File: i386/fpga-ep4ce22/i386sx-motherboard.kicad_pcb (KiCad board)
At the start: 6 copper layers, 88.8 x 70.2 mm, 148 parts, among them J1 HR911105A, J2 PJ-063AH 12V, J3 JTAG, J4 SPI ISP, J5 UART, U1 NG80386SX-20, U10 TLV62569DBVR VCCAUX, U11 SN74LVC8T245PWR, U12 SN74LVC8T245PWR, U13 SN74LVC8T245PWR, U14 SN74LVC8T245PWR, U15 SN74LVC8T245PWR, U16 SN74LVC8T245PWR, U2 SN74AHCT1G125DBVR, U3 EP4CE22F17C8N, U4 W9825G6KH-6I, U5 W25Q64FVDAIG (DIP-8, socketed), U6 LAN8720A-CP-TR, U7 TPS5430DDAR 12->5V, U8 TPS54620RGYR 12->3V3, U9 TPS62130RGTR VCCINT, Y1 25MHz XO, Y2 25MHz

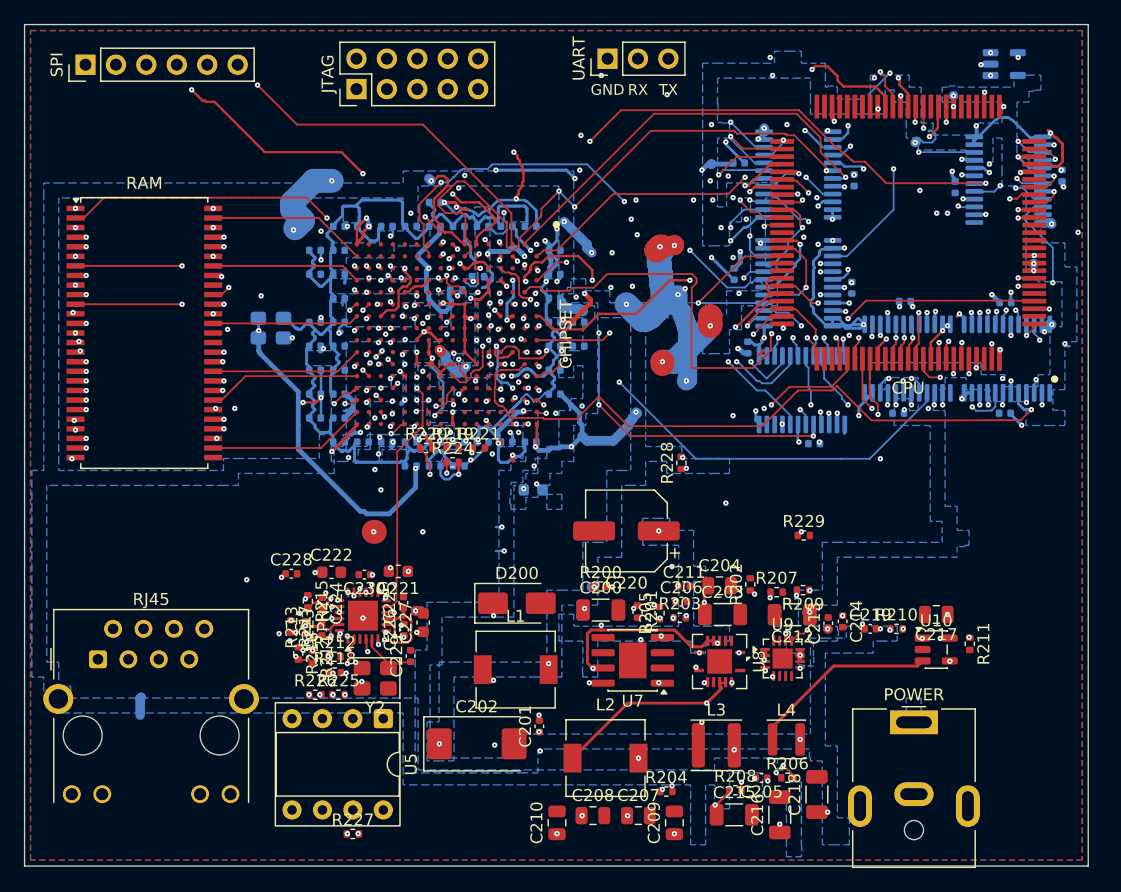
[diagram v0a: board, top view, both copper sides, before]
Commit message: Publish the motherboards' KiCad files
From socket3@c0f6464 socket7@9205469 socket370@524f5b1 i386@bea926c
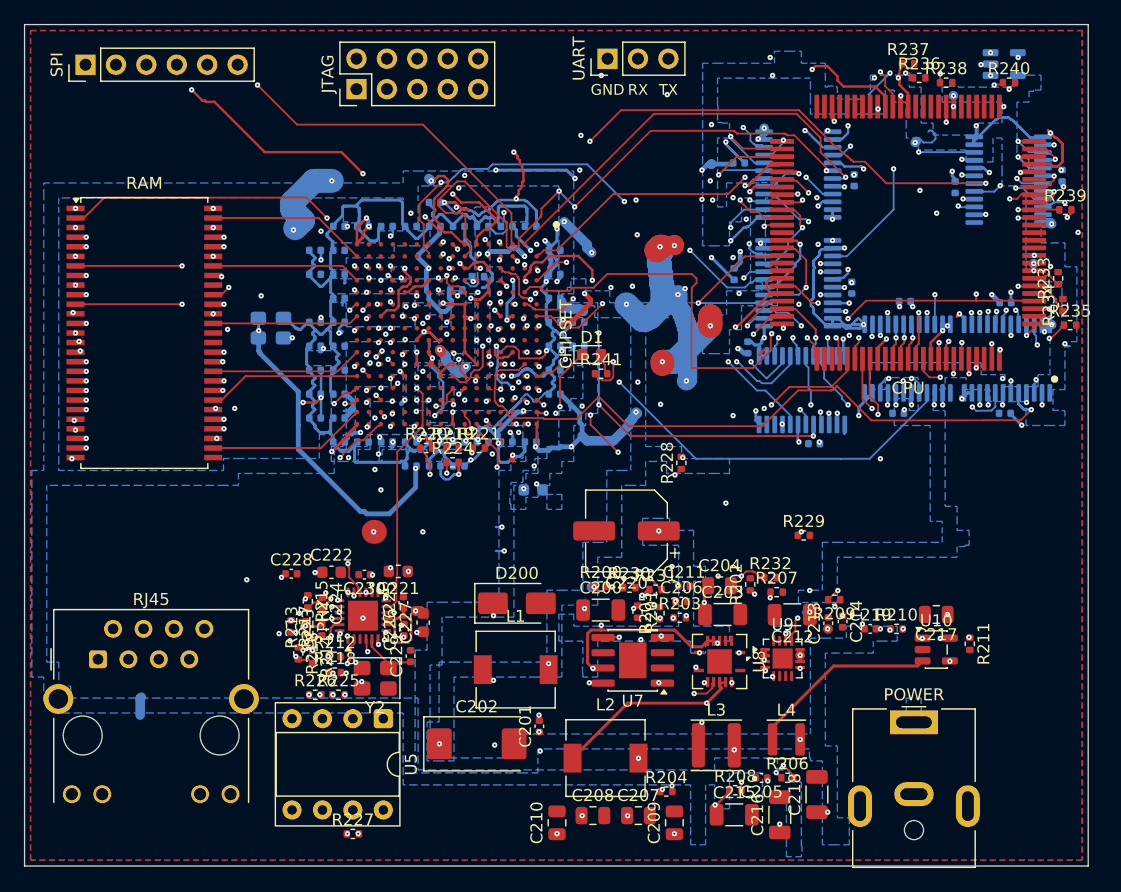
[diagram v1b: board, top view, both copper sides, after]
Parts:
- added D1: red LED KT-0603R, LED_0603_1608Metric, F.Cu at (83.6, 45.2)
- added R230: 1k 1%, R_0402_1005Metric, F.Cu at (86.8, 64.7)
- added R231: 316k 1%, R_0402_1005Metric, F.Cu at (88.9, 64.8)
- added R232: 46.4k 1%, R_0402_1005Metric, F.Cu at (98.5, 63.8)
- added R233: 1k 1%, R_0402_1005Metric, F.Cu at (122.5, 38.8)
- added R234: 1k 1%, R_0402_1005Metric, F.Cu at (122.9, 41.1)
- added R235: 1k 1%, R_0402_1005Metric, F.Cu at (123.5, 42.7)
- added R236: 1k 1%, R_0402_1005Metric, F.Cu at (110.9, 22.1)
- added R237: 1k 1%, R_0402_1005Metric, F.Cu at (110.0, 20.9)
- added R238: 1k 1%, R_0402_1005Metric, F.Cu at (113.2, 22.5)
- added R239: 21.5k 1%, R_0402_1005Metric, F.Cu at (123.1, 33.1)
- added R240: 21.5k 1%, R_0402_1005Metric, F.Cu at (118.4, 22.5)
- added R241: 330R 1%, R_0402_1005Metric, F.Cu at (84.4, 46.8)
- moved R209 2.72 mm to (103.8, 65.7)
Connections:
- C212 pad 1: +5V -> +3V3
- C213 pad 1: +5V -> +3V3
- R209 pad 1: +5V -> +3V3
- U1 pad 28: cpu_flt_n -> (no net)
- U1 pad 34: cpu_busy_n -> (no net)
- U1 pad 36: cpu_error_n -> (no net)
- U1 pad 37: cpu_pereq -> (no net)
- U3 pad A6: cpu_busy_n -> (no net)
- U3 pad A7: cpu_flt_n -> cpu_ready_n
- U3 pad A9: cpu_ready_n -> (no net)
- U3 pad B6: cpu_error_n -> fpga_xlat_oe_n
- U3 pad B9: fpga_xlat_oe_n -> (no net)
- U3 pad E7: cpu_pereq -> (no net)
- U3 pad G15: (no net) -> led_n
- U3 pad G16: (no net) -> cpu_pwr_en
- U3 pad M16: eth_rmii_tx_en -> (no net)
- U3 pad P16: (no net) -> eth_rmii_tx_en
- U7 pad 5: (no net) -> cpu_pwr_en
- U8 pad 10: (no net) -> u8_en
- U9 pad 10: +5V -> +3V3
- U9 pad 11: +5V -> +3V3
- U9 pad 12: +5V -> +3V3
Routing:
- net cpu_flt_n: track 54.4 -> 0.00 mm, vias 4 -> 0
- net cpu_pereq: track 48.3 -> 0.00 mm, vias 2 -> 0
- net cpu_error_n: track 43.5 -> 0.00 mm, vias 5 -> 0
- net cpu_busy_n: track 42.8 -> 0.00 mm, vias 2 -> 0
- net cpu_pwr_en: track 0.00 -> 27.1 mm, vias 0 -> 3
- net u8_en: track 0.00 -> 24.7 mm, vias 0 -> 4
- net led_n: track 0.00 -> 18.4 mm, vias 0 -> 2
- net +3V3: track 435.1 -> 448.0 mm, vias 80 -> 85
- net cpu_hold: track 46.9 -> 57.2 mm, vias 2 -> 4
- net fpga_xlat_oe_n: track 131.0 -> 141.2 mm
- net cpu_ready_n: track 43.7 -> 49.0 mm
- net cpu_reset: track 51.2 -> 56.2 mm, vias 2 -> 3
- net cpu_na_n: track 45.4 -> 49.1 mm
- net cpu_intr: track 43.8 -> 47.1 mm, vias 3 -> 4
- net cpu_lock_n: track 6.90 -> 9.82 mm, vias 2 -> 3
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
